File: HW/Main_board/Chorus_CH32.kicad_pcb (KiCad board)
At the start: 2 copper layers, 31.2 x 74 mm, 88 parts, among them J1 DC_Jack, J2 Prog_Head, J3 Footswitch, J4 IN, J5 OUT, J6 Pot1, J7 Pot2, J8 UART, J9 9V, K1 G6KU-2, U1 AMS1117-5.0, U4 74LVC2G00, U6 TL072, U7 TL072, U8 TL072, U9 CH32V003AxMx

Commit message: working passthrough code with dma + ouput buffer HW
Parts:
- removed C14: 100n, Capacitor_SMD:C_0603_1608Metric
- removed C15, C18: 22n, Capacitor_SMD:C_0603_1608Metric
- removed C16: 2n2, Capacitor_SMD:C_0603_1608Metric
- removed C17: 33n, Capacitor_SMD:C_0603_1608Metric
- removed C19: 10u, Capacitor_SMD:CP_Elec_5x5.4
- removed R11: 2k2, Resistor_SMD:R_0603_1608Metric
- removed R12: 4k7, Resistor_SMD:R_0603_1608Metric
- removed R13, R18: 100k, Resistor_SMD:R_0603_1608Metric
- removed R14, R17: 47k, Resistor_SMD:R_0603_1608Metric
- removed R15: 6k8, Resistor_SMD:R_0603_1608Metric
- removed R16: 3k3, Resistor_SMD:R_0603_1608Metric
- removed R19: 1k, Resistor_SMD:R_0603_1608Metric
- J3, J4, J5: footprint Connector_JST:JST_PH_B2B-PH-K_1x02_P2.00mm_Vertical -> Connector_PinHeader_2.54mm:PinHeader_1x02_P2.54mm_Vertical
- J6, J7: footprint Connector_JST:JST_PH_B3B-PH-K_1x03_P2.00mm_Vertical -> Connector_PinHeader_2.54mm:PinHeader_1x02_P2.54mm_Vertical
- J9: footprint Connector_JST:JST_PH_B2B-PH-K_1x02_P2.00mm_Vertical -> Connector_PinSocket_2.54mm:PinSocket_1x02_P2.54mm_Vertical
- moved D1 11.9 mm to (116.8, 73.1), turned to 180 degrees
- moved J2 2.04 mm to (163.2, 82.2)
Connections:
- J2 pad 1: +5V -> unconnected-(J2-Pin_1-Pad1)
- U7 pad 1: Net-(U7A--) -> (no net)
- U7 pad 2: Net-(U7A--) -> (no net)
- U7 pad 3: Net-(U7A-+) -> (no net)
- U7 pad 5: Vref -> (no net)
- U7 pad 6: Net-(U7B--) -> (no net)
- U7 pad 7: Net-(C18-Pad2) -> (no net)

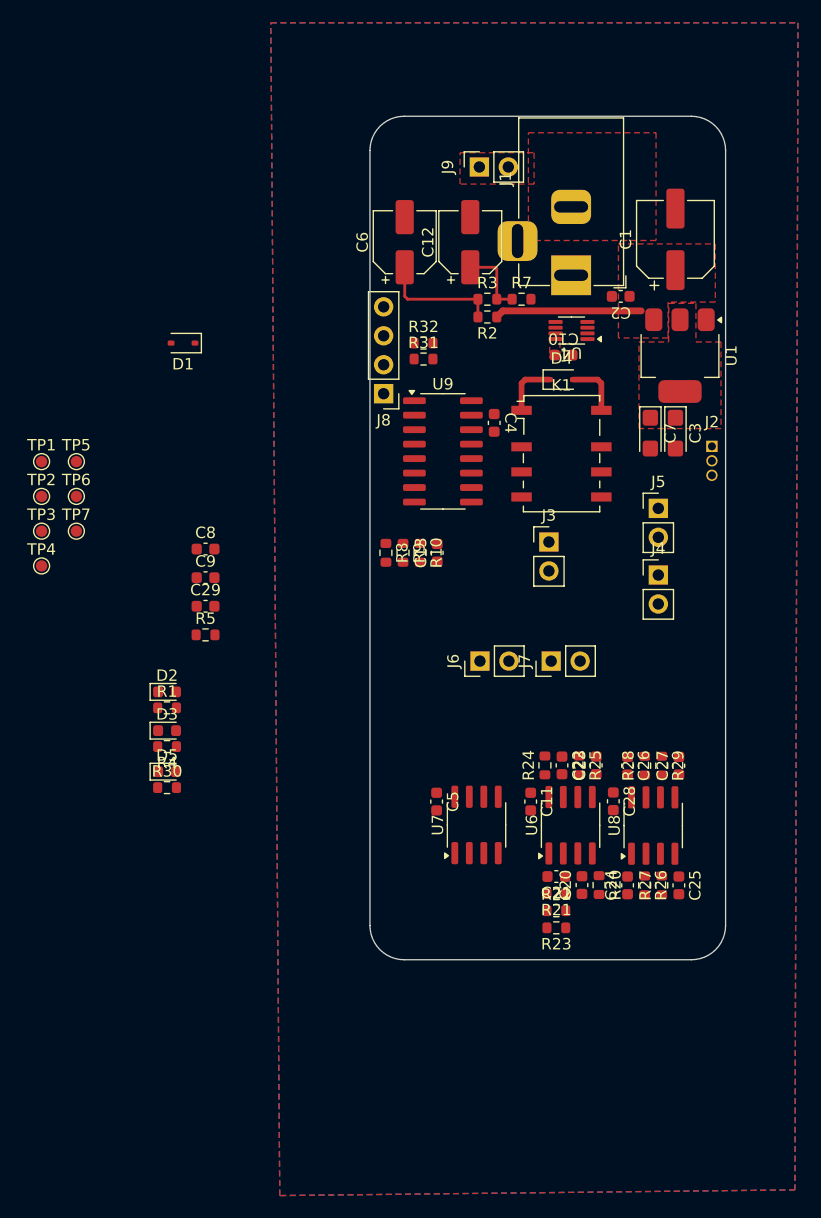
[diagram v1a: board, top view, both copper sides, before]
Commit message: correction on output board and new main layout/schem
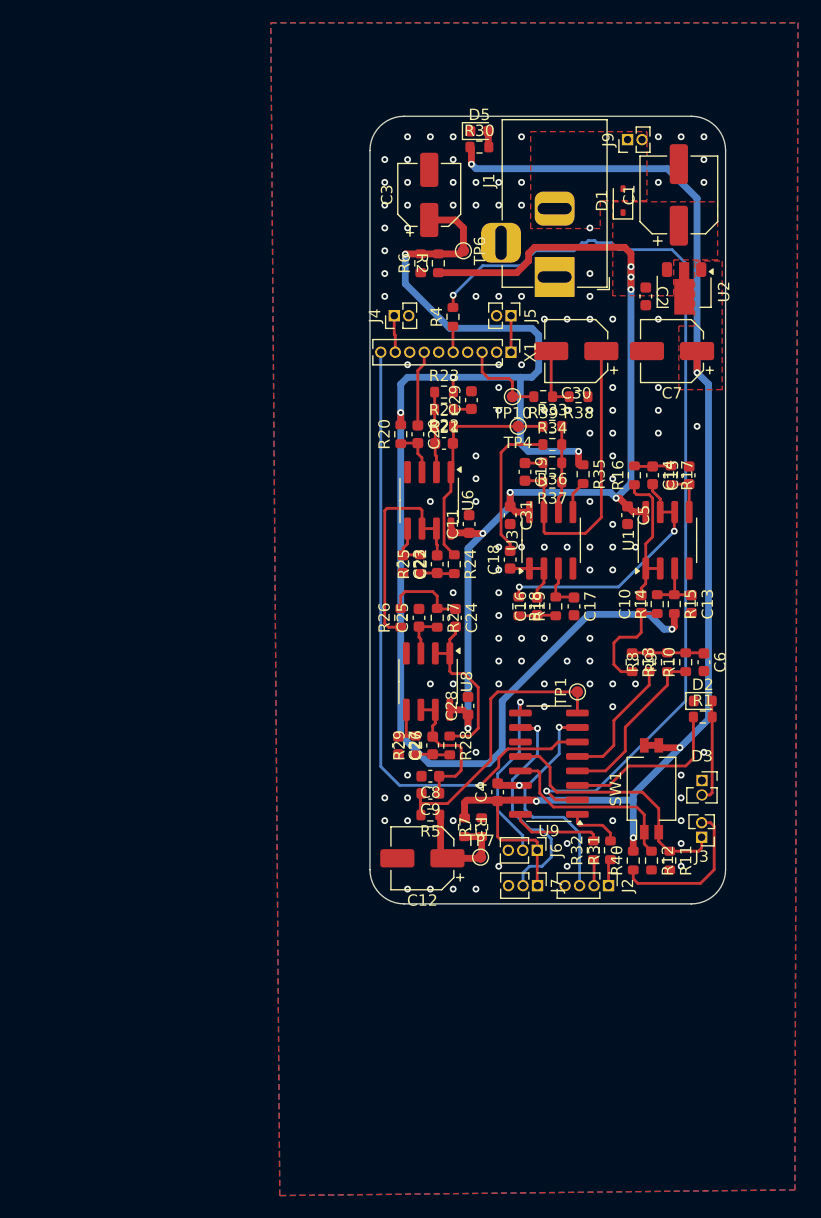
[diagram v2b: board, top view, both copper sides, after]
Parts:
- removed D4: 1N5819WS, Diode_SMD:D_SOD-323
- removed J8: UART, Connector_PinHeader_2.54mm:PinHeader_1x04_P2.54mm_Vertical
- removed K1: G6KU-2, Relay_SMD:Relay_DPDT_Omron_G6K-2F-Y
- removed TP2, TP3, TP5: TestPoint, TestPoint:TestPoint_Pad_D1.0mm
- removed U4: 74LVC2G00, Package_SO:VSSOP-8_2.3x2mm_P0.5mm
- removed U7: TL072, Package_SO:SOIC-8_3.9x4.9mm_P1.27mm
- added C14: 1n, Capacitor_SMD:C_0603_1608Metric, F.Cu at (158.0, 84.7)
- added C15: 150p, Capacitor_SMD:C_0603_1608Metric, F.Cu at (161.2, 84.7)
- added C16: 1n, Capacitor_SMD:C_0603_1608Metric, F.Cu at (147.9, 96.2)
- added C17: 470p, Capacitor_SMD:C_0603_1608Metric, F.Cu at (151.1, 96.2)
- added C18: 33n, Capacitor_SMD:C_0603_1608Metric, F.Cu at (145.5, 92.1)
- added C19: 22n, Capacitor_SMD:C_0603_1608Metric, F.Cu at (146.8, 84.4)
- added C30: 10u, Capacitor_SMD:CP_Elec_5x5.4, F.Cu at (151.3, 73.8)
- added C31: 100n, Capacitor_SMD:C_0603_1608Metric, F.Cu at (145.5, 88.2)
- added R11: 10k, Resistor_SMD:R_0603_1608Metric, F.Cu at (159.5, 118.5)
- added R12: 10k, Resistor_SMD:R_0603_1608Metric, F.Cu at (157.9, 118.5)
- added R13: 4k7, Resistor_SMD:R_0603_1608Metric, F.Cu at (156.2, 101.1)
- added R14: 47k, Resistor_SMD:R_0603_1608Metric, F.Cu at (158.4, 96.0)
- added R15: 150k, Resistor_SMD:R_0603_1608Metric, F.Cu at (159.9, 96.0)
- added R16: 22k, Resistor_SMD:R_0603_1608Metric, F.Cu at (156.4, 84.7)
- added R17: 47k, Resistor_SMD:R_0603_1608Metric, F.Cu at (159.6, 84.7)
- added R18: 22k, Resistor_SMD:R_0603_1608Metric, F.Cu at (146.3, 96.2)
- added R19: 47k, Resistor_SMD:R_0603_1608Metric, F.Cu at (149.5, 96.2)
- added R33: 47k, Resistor_SMD:R_0603_1608Metric, F.Cu at (149.2, 80.4)
- added R34: 47k, Resistor_SMD:R_0603_1608Metric, F.Cu at (149.2, 82.0)
- added R35: 10k, Resistor_SMD:R_0603_1608Metric, F.Cu at (151.9, 84.6)
- added R36: 3k3, Resistor_SMD:R_0603_1608Metric, F.Cu at (149.2, 83.6)
- added R37: 47k, Resistor_SMD:R_0603_1608Metric, F.Cu at (149.2, 85.3)
- added R38: 150k, Resistor_SMD:R_0603_1608Metric, F.Cu at (151.5, 77.8)
- added R39: 1k, Resistor_SMD:R_0603_1608Metric, F.Cu at (148.4, 77.8)
- added R40: 10k, Resistor_SMD:R_0603_1608Metric, F.Cu at (156.3, 118.5)
- added R6: 10k, Resistor_SMD:R_0603_1608Metric, F.Cu at (137.7, 66.1)
- added SW1: MODE, Button_Switch_SMD:SW_DIP_SPSTx02_Slide_KingTek_DSHP02TS_W7.62mm_P1.27mm, F.Cu at (157.9, 112.2)
- added TP10: TestPoint, TestPoint:TestPoint_Pad_D1.0mm, F.Cu at (145.7, 77.8)
- added U2: L78L05_SOT89, Package_TO_SOT_SMD:SOT-89-3, F.Cu at (160.8, 68.6)
- added U3: TL072, Package_SO:SOIC-8_3.9x4.9mm_P1.27mm, F.Cu at (149.1, 90.4)
- added X1: ~, Connector_PinHeader_1.27mm:PinHeader_1x10_P1.27mm_Vertical, F.Cu at (145.6, 73.9)
- C10: value 100n -> 1n
- C13: value 15n -> 100p
- C3, C7: footprint Capacitor_Tantalum_SMD:CP_EIA-3216-18_Kemet-A -> Capacitor_SMD:CP_Elec_5x5.4
- C6: value 10u -> 10n; footprint Capacitor_SMD:CP_Elec_5x5.4 -> Capacitor_SMD:C_0603_1608Metric
- D3: value LED -> CTL1; footprint LED_SMD:LED_0603_1608Metric -> Connector_PinSocket_1.27mm:PinSocket_1x02_P1.27mm_Vertical
- J2: footprint Connector_PinSocket_1.27mm:PinSocket_1x03_P1.27mm_Vertical -> Connector_PinHeader_1.27mm:PinHeader_1x04_P1.27mm_Vertical
- J3: value Footswitch -> SW; footprint Connector_PinHeader_2.54mm:PinHeader_1x02_P2.54mm_Vertical -> Connector_PinHeader_1.27mm:PinHeader_1x02_P1.27mm_Vertical
- J4, J5: footprint Connector_PinHeader_2.54mm:PinHeader_1x02_P2.54mm_Vertical -> Connector_PinHeader_1.27mm:PinHeader_1x02_P1.27mm_Vertical
- J6, J7: footprint Connector_PinHeader_2.54mm:PinHeader_1x02_P2.54mm_Vertical -> Connector_PinHeader_1.27mm:PinHeader_1x03_P1.27mm_Vertical
- J9: footprint Connector_PinSocket_2.54mm:PinSocket_1x02_P2.54mm_Vertical -> Connector_PinHeader_1.27mm:PinHeader_1x02_P1.27mm_Vertical
- R10: value 2k2 -> 150k
- R2: value 27k -> 10k
- R21: value 8.2k -> 33k
- R22: value 2.7k -> 3k3
- R7: value 15k -> 10k
- R8: value 2M2 -> 2k2
- R9: value 150k -> 3k3
- TP6: value TestPoint -> Vref
- TP7: value TestPoint -> 2V5
- U1: value AMS1117-5.0 -> TL072; footprint Package_TO_SOT_SMD:SOT-223-3_TabPin2 -> Package_SO:SOIC-8_3.9x4.9mm_P1.27mm
- moved D5 62.5 mm to (142.8, 54.5)
- moved R30 62.5 mm to (142.8, 55.9)
- moved C12 54.2 mm to (137.8, 118.3), turned to 180 degrees
- moved TP1 51.2 mm to (151.4, 103.7), turned to 90 degrees
- moved R23 48.0 mm to (139.7, 77.4), turned to 0 degrees
- moved D3 47.1 mm to (162.3, 111.5)
- moved D2 47.0 mm to (162.4, 104.5)
- moved R1 47.0 mm to (162.4, 105.9)
- moved R32 46.9 mm to (152.8, 117.6), turned to 90 degrees
- moved R7 46.5 mm to (143.0, 115.6), turned to 90 degrees
- moved R3 46.4 mm to (141.5, 115.6), turned to -90 degrees
- moved R31 46.1 mm to (154.3, 117.6), turned to 90 degrees
- moved TP7 45.6 mm to (142.9, 118.2)
- moved R4 45.3 mm to (140.5, 70.8), turned to 90 degrees
- moved C6 45.2 mm to (162.5, 101.1), turned to -90 degrees
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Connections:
- net Net-(U9-PC3) renamed /LED
- C10 pad 1: +5V -> Net-(C10-Pad1)
- C10 pad 2: GND -> Net-(U1A--)
- C13 pad 1: Net-(C13-Pad1) -> Net-(U1A-+)
- C3 pad 1: +5V -> Vref
- C6 pad 1: Vref -> Net-(C6-Pad1)
- D3 pad 2: Net-(D3-A) -> Net-(D2-A)
- J2 pad 1: unconnected-(J2-Pin_1-Pad1) -> Net-(J2-Pin_1)
- J2 pad 2: /SWDIO -> Net-(J2-Pin_2)
- J2 pad 3: GND -> /SWDIO
- J3 pad 1: +5V -> /DIP0
- J3 pad 2: /SWITCH_OUT -> Net-(J3-Pin_2)
- R10 pad 1: /PWM_OUT_2 -> /PWM_OUT_1
- R10 pad 2: Net-(C13-Pad1) -> Net-(C6-Pad1)
- R3 pad 1: Vref -> +5V
- R31 pad 1: Net-(J8-Pin_2) -> Net-(J2-Pin_1)
- R31 pad 2: /TX -> /RX
- R32 pad 1: Net-(J8-Pin_3) -> Net-(J2-Pin_2)
- R32 pad 2: /RX -> /TX
- R4 pad 1: Net-(D3-A) -> /LED_SW
- R8 pad 1: /PWM_OUT_1 -> /PWM_OUT_2
- R8 pad 2: Net-(C13-Pad1) -> Net-(C6-Pad1)
- R9 pad 2: Net-(C13-Pad1) -> Net-(C6-Pad1)
- U1 pad 1: GND -> Net-(U1A--)
- U1 pad 2: +5V -> Net-(U1A--)
- U1 pad 3: +9V -> Net-(U1A-+)
- U9 pad 12: Net-(U9-PA1) -> /DIP0
- U9 pad 13: Net-(U9-PA2) -> /DIP1
- U9 pad 6: /SWITCH_OUT -> /~{SW_STATE}
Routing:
- net +5V: track 0.18 -> 115.3 mm, vias 0 -> 5
- net Vref: track 10.6 -> 122.9 mm, vias 0 -> 5
- net Net-(U9-PC2): track 0.00 -> 81.2 mm, vias 0 -> 2
- net +9V: track 12.9 -> 85.7 mm, vias 0 -> 7
- net /~{SW_STATE}: track 0.00 -> 56.3 mm, vias 0 -> 1
- net Net-(C19-Pad2): track 0.00 -> 26.3 mm
- net /ADC_IN: track 0.00 -> 24.8 mm
- net /DIP0: track 0.00 -> 23.0 mm
- net Net-(U1B--): track 0.00 -> 22.2 mm, vias 0 -> 2
- net /SWDIO: track 0.00 -> 20.3 mm, vias 0 -> 1
- net Net-(U6B--): track 0.00 -> 20.1 mm
- net /POT_2: track 0.00 -> 19.9 mm, vias 0 -> 1
- net /DRY: track 0.00 -> 19.8 mm
- net /DIP1: track 0.00 -> 17.0 mm
- net /POT_1: track 0.00 -> 15.7 mm, vias 0 -> 1
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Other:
- board size 31.2 x 74 mm -> 31.2 x 69.1 mm

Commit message: silkscreen ok
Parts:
- added C32: 100n, Capacitor_SMD:C_0603_1608Metric, F.Cu at (142.7, 121.3)
- added C33: 100n, Capacitor_SMD:C_0603_1608Metric, F.Cu at (161.3, 78.8)
- added C34: 10u, Capacitor_SMD:C_0603_1608Metric, F.Cu at (142.7, 119.9)
- added C35: 10u, Capacitor_SMD:C_0603_1608Metric, F.Cu at (163.1, 78.8)
- added C36: 10u, Capacitor_SMD:C_0603_1608Metric, F.Cu at (136.2, 66.1)
- added C37: 100n, Capacitor_SMD:C_0603_1608Metric, F.Cu at (134.7, 66.1)
- added C38: 10u, Capacitor_SMD:C_0603_1608Metric, F.Cu at (155.9, 69.0)
- added C39: 100p, Capacitor_SMD:C_0603_1608Metric, F.Cu at (149.2, 84.3)
- added R41: 33, Resistor_SMD:R_0603_1608Metric, F.Cu at (155.2, 107.0)
- added R42: 33, Resistor_SMD:R_0603_1608Metric, F.Cu at (153.6, 107.0)
- C1: value 100u -> 220u
- C12, C7: value 10u -> 22u
- moved R36 0.70 mm to (149.2, 82.9)
- moved R34 0.60 mm to (149.2, 81.4)
- moved R37 0.55 mm to (149.2, 85.8)
- moved R33 0.50 mm to (149.2, 79.9)
- moved TP7 0.40 mm to (142.9, 117.8)
- moved C12 0.15 mm to (137.8, 118.2)
- renumbered J2 to DEBUG, SW1 to MODE, J6 to POT, J7 to POT2
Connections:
- U9 pad 4: /PWM_OUT_1 -> Net-(U9-PC4)
- U9 pad 5: /PWM_OUT_2 -> Net-(U9-PC6)
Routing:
- net /PWM_OUT_1: track 15.0 -> 8.62 mm
- net Net-(U9-PC4): track 0.00 -> 5.72 mm
- net /PWM_OUT_2: track 11.4 -> 7.30 mm
- net Vref: track 122.9 -> 126.4 mm
- net 2V5: track 10.5 -> 13.9 mm
- net Net-(U9-PC6): track 0.00 -> 3.41 mm
- net Net-(C19-Pad2): track 26.3 -> 27.5 mm
- net +9V: track 85.7 -> 84.9 mm
- net Net-(C19-Pad1): track 1.59 -> 2.18 mm
- net GND: vias 117 -> 113
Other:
- board text added: "+"
- board text added: "-"
- board text added: "1"
- board text added: "2"
- board text added: "3PDT"
- board text added: "CHorus32 rev1"
- board text added: "IN"
- board text added: "INFX"
- board text added: "IO"
- board text added: "JLCJLCJLCJLC"
- board text added: "LED"
- board text added: "MODE"
- board text added: "O"
- board text added: "OFX"
- board text added: "RX"
- board text added: "SW"
- board text added: "TX"

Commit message: moved spdt connector
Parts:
- moved X1 0.12 mm to (145.7, 73.9)
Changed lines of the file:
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@@
 	(footprint "Connector_PinHeader_1.27mm:PinHeader_1x10_P1.27mm_Vertical"
 		(layer "F.Cu")
-		(at 145.58 73.9 -90)
+		(at 145.7 73.9 -90)
 		(descr "Through hole straight pin header, 1x10, 1.27mm pitch, single row")
 		(tags "Through hole pin header THT 1x10 1.27mm single row")
@@
 	)
 	(segment
-		(start 135.42 72.42)
-		(end 135.42 73.9)
+		(start 135.54 72.54)
+		(end 135.54 73.9)
 		(width 0.25)
 		(layer "F.Cu")
@@
 	)
 	(segment
-		(start 135.33 70.7)
-		(end 135.33 72.33)
+		(start 135.33 72.33)
+		(end 135.54 72.54)
 		(width 0.25)
 		(layer "F.Cu")
@@
 	)
 	(segment
-		(start 135.33 72.33)
-		(end 135.42 72.42)
+		(start 135.33 70.7)
+		(end 135.33 72.33)
 		(width 0.25)
 		(layer "F.Cu")
@@
 	)
 	(segment
-		(start 140.48 71.625)
-		(end 140.48 73.88)
+		(start 140.48 73.76)
+		(end 140.62 73.9)
 		(width 0.25)
 		(layer "F.Cu")
@@
 	)
 	(segment
-		(start 140.48 73.88)
-		(end 140.5 73.9)
+		(start 140.48 71.625)
+		(end 140.48 73.76)
 		(width 0.25)
 		(layer "F.Cu")
@@
 	)
 	(segment
-		(start 137.96 73.9)
-		(end 137.96 74.94)
+		(start 138.08 73.9)
+		(end 138.08 74.82)
 		(width 0.25)
 		(layer "F.Cu")
@@
 	)
 	(segment
-		(start 137.96 74.94)
+		(start 138.08 74.82)
 		(end 137.4 75.5)
 		(width 0.25)
@@
 	)
 	(segment
+		(start 145.58 73.78)
+		(end 145.7 73.9)
+		(width 0.25)
+		(layer "F.Cu")
+		(net 13)
+	)
+	(segment
 		(start 145.58 70.7)
-		(end 145.58 73.9)
+		(end 145.58 73.78)
 		(width 0.25)
 		(layer "F.Cu")
@@
 	)
 	(segment
-		(start 135.8 111.9)
-		(end 142.9 111.9)
+		(start 134.15 110.25)
+		(end 135.8 111.9)
 		(width 0.25)
 		(layer "B.Cu")
@@
 	)
 	(segment
-		(start 134.15 110.25)
-		(end 135.8 111.9)
+		(start 134.27 73.9)
+		(end 134.15 74.02)
 		(width 0.25)
 		(layer "B.Cu")
@@
 	)
 	(segment
-		(start 134.15 73.9)
+		(start 134.15 74.02)
 		(end 134.15 110.25)
 		(width 0.25)
@@
 	)
 	(segment
+		(start 135.8 111.9)
+		(end 142.9 111.9)
+		(width 0.25)
+		(layer "B.Cu")
+		(net 34)
+	)
+	(segment
 		(start 153.6 104.7)
 		(end 153.6 106.175)
@@
 	)
 	(segment
-		(start 147.575 77.8)
-		(end 145.7 77.8)
+		(start 145.7 77.8)
+		(end 145.7 76.5)
 		(width 0.25)
 		(layer "F.Cu")
@@
 	)
 	(segment
-		(start 143.04 75.64)
-		(end 143.04 73.9)
+		(start 145.7 76.5)
+		(end 145.4 76.2)
 		(width 0.25)
 		(layer "F.Cu")
@@
 	)
 	(segment
-		(start 145.4 76.2)
-		(end 143.6 76.2)
+		(start 147.575 77.8)
+		(end 145.7 77.8)
 		(width 0.25)
 		(layer "F.Cu")
@@
 	(segment
 		(start 143.6 76.2)
-		(end 143.04 75.64)
+		(end 143.16 75.76)
 		(width 0.25)
 		(layer "F.Cu")
@@
 	)
 	(segment
-		(start 145.7 76.5)
-		(end 145.4 76.2)
+		(start 145.4 76.2)
+		(end 143.6 76.2)
 		(width 0.25)
 		(layer "F.Cu")
@@
 	)
 	(segment
-		(start 145.7 77.8)
-		(end 145.7 76.5)
+		(start 143.16 75.76)
+		(end 143.16 73.9)
 		(width 0.25)
 		(layer "F.Cu")
